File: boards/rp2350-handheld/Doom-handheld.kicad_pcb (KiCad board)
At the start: 2 copper layers, 160 x 86 mm, 13 parts, among them U1 PIM724

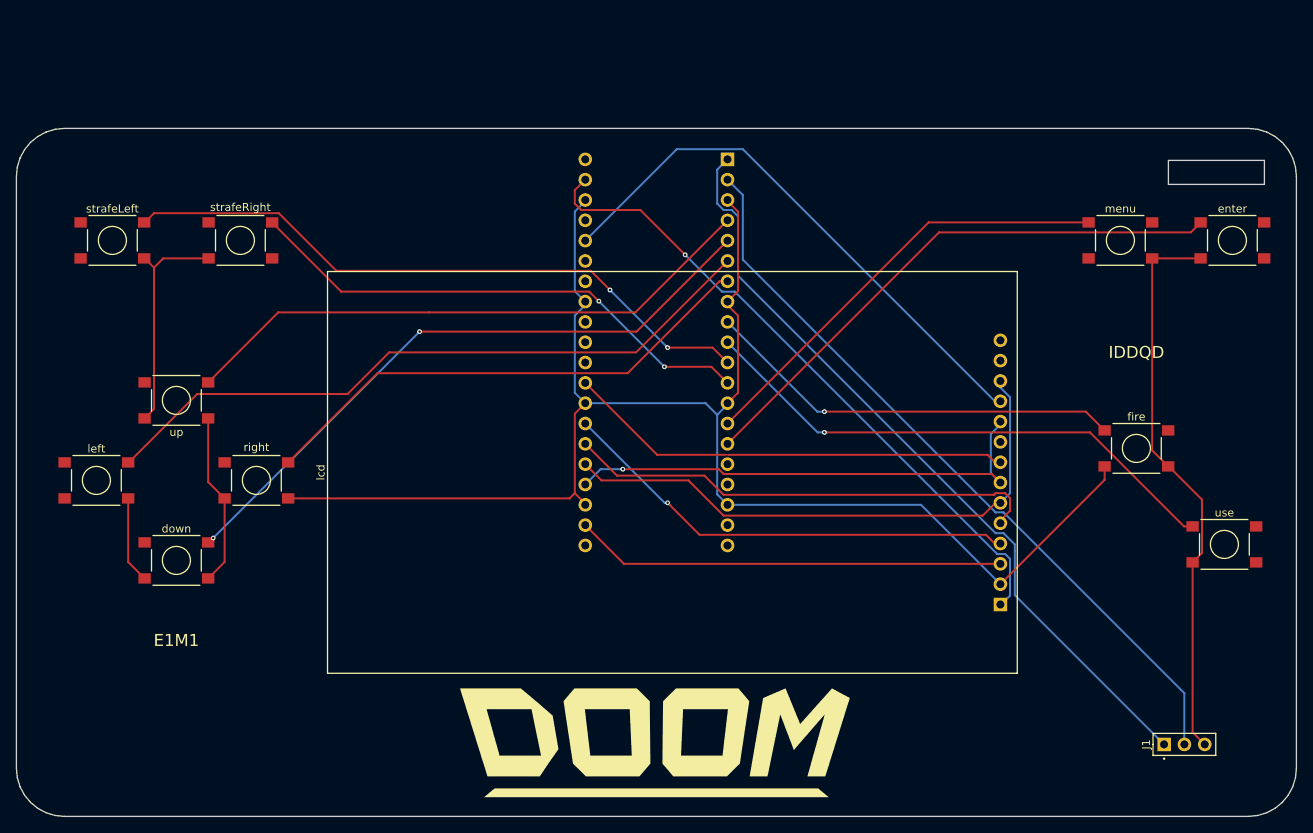
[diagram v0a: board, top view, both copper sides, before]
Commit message: PCBKit's mark and pcbkit.io on every board; the RP2350 handheld ready to order
The handheld runs from two 18650 cells in parallel behind a DW01A protector and a reverse-cell
P-MOSFET, charged at up to 500 mA from the Pico's USB-C by a BQ24075 (power path into VSYS, timers
off for 6 Ah), with an on/off switch on 3V3_EN, M3 holes, ground pours and the console on pads.
Every assembled part has a JLCPCB code in stock (Basic where there is one); the module sockets are
in the BOM, the modules listed in the order's README. Check complete, the ready review clean.
Every board: routed and checked complete with the new mark.
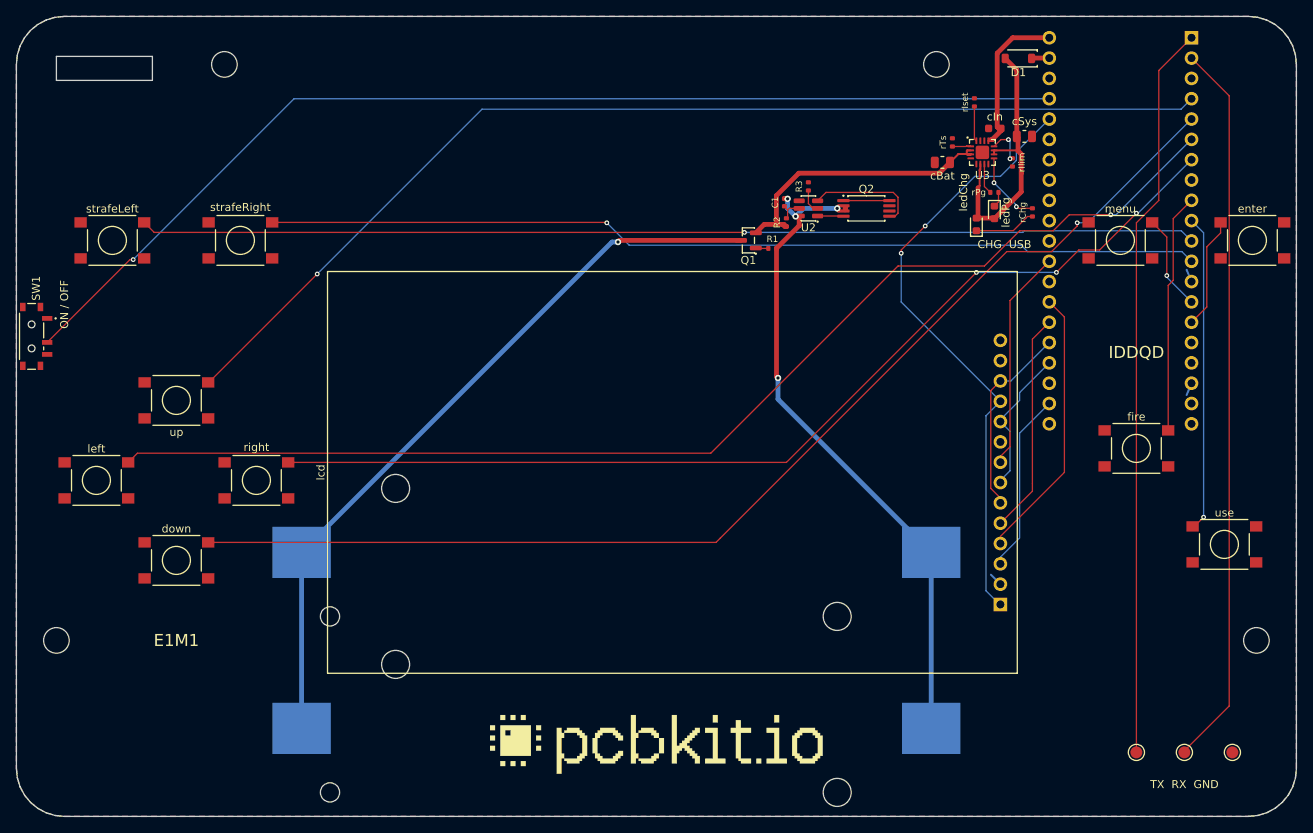
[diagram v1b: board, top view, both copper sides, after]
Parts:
- removed J1: , PinHeader_1x03_P2.54mm_Vertical
- added BT1: 1042, BatteryHolder_Keystone_1042_1x18650, B.Cu at (175.0, 189.0)
- added BT2: 1042, BatteryHolder_Keystone_1042_1x18650, B.Cu at (175.0, 167.0)
- added C1: 100nF, C_0402_1005Metric, F.Cu at (196.0, 123.2)
- added D1: 1N5819HW-7-F, D_SOD-123, F.Cu at (225.2, 105.2)
- added H1: , MountingHole_3.2mm_M3, F.Cu at (105.0, 178.0)
- added H2: , MountingHole_3.2mm_M3, F.Cu at (255.0, 178.0)
- added H3: , MountingHole_3.2mm_M3, F.Cu at (126.0, 106.0)
- added H4: , MountingHole_3.2mm_M3, F.Cu at (215.0, 106.0)
- added Q1: AO3401A, SOT-23, F.Cu at (191.5, 128.0)
- added Q2: FS8205A, TSSOP-8_4.4x2.93mm_P0.65mm, F.Cu at (206.2, 124.0)
- added R1: 100kohm, R_0402_1005Metric, F.Cu at (194.5, 129.0)
- added R2: 100ohm, R_0402_1005Metric, F.Cu at (196.2, 125.8)
- added R3: 1kohm, R_0402_1005Metric, F.Cu at (199.0, 121.2)
- added SW1: MSK12C02, SW_Slide_SPDT_Shouhan_MSK12C02, F.Cu at (101.9, 140.0)
- added U2: DW01A, SOT-6_1.6x2.9mm_P0.95mm, F.Cu at (199.0, 124.0)
- added U3: BQ24075RGTR, QFN-16-1EP_3x3mm_P0.5mm_EP1.68x1.68mm, F.Cu at (220.8, 117.0)
- added cBat: 4.7uF, C_0805_2012Metric, F.Cu at (215.8, 118.2)
- added cIn: 1uF, C_0603_1608Metric, F.Cu at (222.3, 114.0)
- added cSys: 4.7uF, C_0805_2012Metric, F.Cu at (226.0, 115.0)
- added ledChg: red, LED_0603_1608Metric, F.Cu at (220.0, 126.0)
- added ledPg: green, LED_0603_1608Metric, F.Cu at (222.2, 124.5)
- added logo: , Logo_PCBKit_pcbkit.io, F.Cu at (180.0, 191.0)
- added rChg: 1.5kohm, R_0402_1005Metric, F.Cu at (227.0, 124.5)
- added rIlim: 1.18kohm, R_0402_1005Metric, F.Cu at (224.5, 118.2)
- added rIset: 1.13kohm, R_0402_1005Metric, F.Cu at (219.8, 110.8)
- added rPg: 1.5kohm, R_0402_1005Metric, F.Cu at (222.2, 122.0)
- added rTs: 10kohm, R_0402_1005Metric, F.Cu at (217.0, 115.8)
- added tpGnd: , TestPoint_Round_D1.5mm, F.Cu at (252.0, 192.0)
- added tpRx: , TestPoint_Round_D1.5mm, F.Cu at (246.0, 192.0)
- added tpTx: , TestPoint_Round_D1.5mm, F.Cu at (240.0, 192.0)
- down, enter, fire, left, menu, right, strafeLeft, strafeRight, up, use: value (none) -> PTS645SM43SMTR92 LFS
- moved U1 60.0 mm to (238.0, 126.8)
- moved enter 2.50 mm to (254.5, 128.0)
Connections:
- U1 pad 37: (no net) -> PWR_EN
- U1 pad 40: (no net) -> VBUS
- lcd pad 1: VSYS -> V3
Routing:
- net GND: track 325.6 -> 4.88 mm
- net PWR_EN: track 0.00 -> 137.9 mm, vias 0 -> 1
- net BAT_IN: track 0.00 -> 93.1 mm, vias 0 -> 1
- net CELL_N: track 0.00 -> 82.8 mm, vias 0 -> 4
- net VSYS: track 82.6 -> 2.23 mm, vias 1 -> 0
- net DOWN: track 79.7 -> 145.1 mm, vias 2 -> 1
- net RIGHT: track 64.3 -> 128.6 mm, vias 0 -> 3
- net UP: track 73.3 -> 137.6 mm, vias 0 -> 1
- net LEFT: track 85.3 -> 149.6 mm, vias 0 -> 1
- net ENTER: track 70.6 -> 14.0 mm
- net STRAFE_R: track 65.2 -> 116.9 mm, vias 2 -> 1
- net STRAFE_L: track 81.1 -> 132.0 mm, vias 2 -> 1
- net LCD_MOSI: track 71.4 -> 24.3 mm
- net MENU: track 55.5 -> 12.0 mm, vias 0 -> 1
- net LCD_SCK: track 62.0 -> 18.5 mm, vias 1 -> 0
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- added copper zone on B.Cu, net GND
- added copper zone on F.Cu, net GND
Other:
- board size 160 x 86 mm -> 160 x 100 mm
- board text added: "+"
- board text added: "-"
- board text added: "2 x 18650 Li-ion 3.7 V"
- board text added: "CHG USB"
- board text added: "ON / OFF"
- board text added: "TX RX GND"
